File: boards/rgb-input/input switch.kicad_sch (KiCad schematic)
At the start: 5 parts, among them J1 Conn_01x02

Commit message: this board is going to be sick.
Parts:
- renumbered D29 to D9
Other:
- moved on the sheet: C3, D9, J1, R1, R2

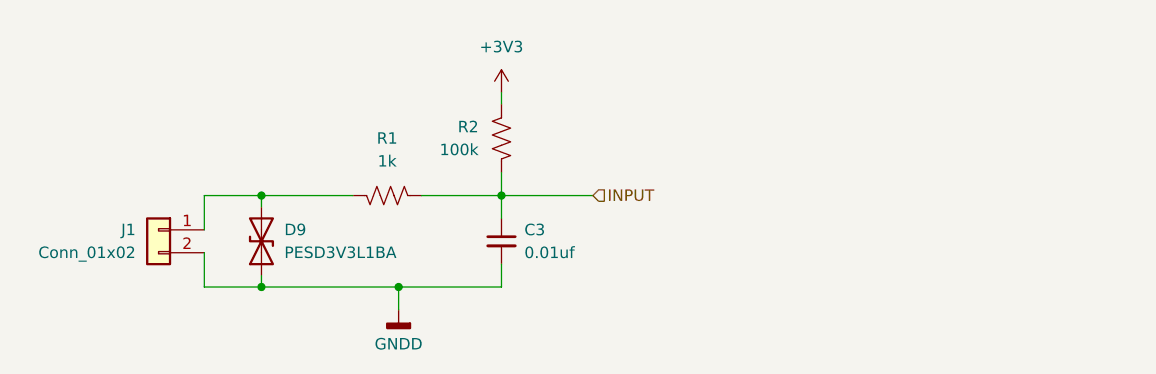
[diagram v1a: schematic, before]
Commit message: tested the bus voltage stuff a bit more
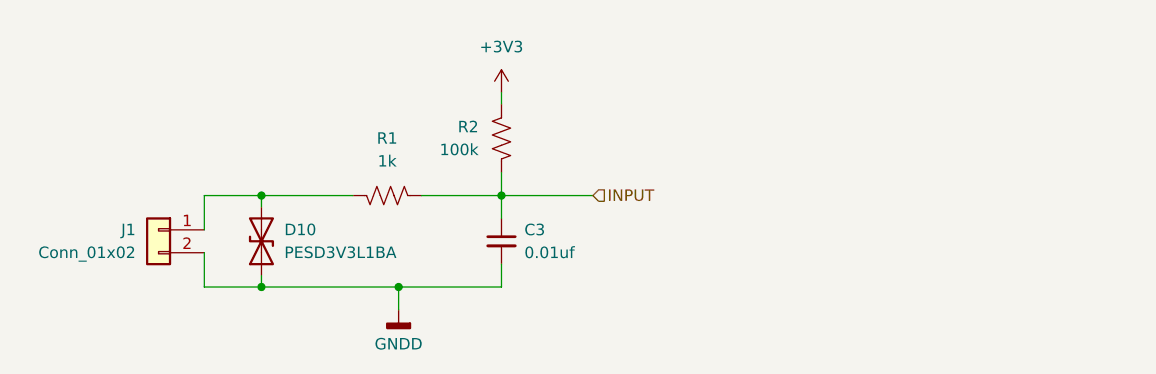
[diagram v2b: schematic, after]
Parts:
- renumbered D9 to D10
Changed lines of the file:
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@@
   (symbol (lib_id "Device:D_TVS") (at 142.24 92.075 90) (unit 1)
     (in_bom yes) (on_board yes) (dnp no)
-    (property "Reference" "D9" (at 144.78 90.805 90)
+    (property "Reference" "D10" (at 144.78 90.805 90)
       (effects (font (size 1.27 1.27)) (justify right))
     )
@@
     (instances
       (project "rgb-input"
+        (path "/c83c6236-96e9-46ad-9d7a-9e2efa4a7966/a581b924-afd8-4b56-b69e-790286072066"
+          (reference "D10") (unit 1)
+        )
+        (path "/c83c6236-96e9-46ad-9d7a-9e2efa4a7966/ef548cdc-9d5d-4f8e-8f54-0c2e96dbe3f0"
+          (reference "D2") (unit 1)
+        )
+        (path "/c83c6236-96e9-46ad-9d7a-9e2efa4a7966/4f50afed-9381-4977-8e27-209f0f88ad4e"
+          (reference "D3") (unit 1)
+        )
+        (path "/c83c6236-96e9-46ad-9d7a-9e2efa4a7966/4175a172-5c0b-4d6a-88bb-129f5f07b813"
+          (reference "D4") (unit 1)
+        )
+        (path "/c83c6236-96e9-46ad-9d7a-9e2efa4a7966/6f6f2d8d-82f6-4691-bba7-8caa1bd52e96"
+          (reference "D5") (unit 1)
+        )
+        (path "/c83c6236-96e9-46ad-9d7a-9e2efa4a7966/145fa34f-e19e-43e2-bb48-aff2e824ef0a"
+          (reference "D6") (unit 1)
+        )
+        (path "/c83c6236-96e9-46ad-9d7a-9e2efa4a7966/5fc618b8-7830-4bbf-bf46-7753631e9b1e"
+          (reference "D7") (unit 1)
+        )
+        (path "/c83c6236-96e9-46ad-9d7a-9e2efa4a7966/802175d5-fb4b-4457-a117-b0f397189ff7"
+          (reference "D8") (unit 1)
+        )
+        (path "/c83c6236-96e9-46ad-9d7a-9e2efa4a7966/0036d08f-39b5-4a29-8e4d-ea832b2cc879"
+          (reference "D29") (unit 1)
+        )
         (path "/c83c6236-96e9-46ad-9d7a-9e2efa4a7966/803edf1a-5825-4947-a8b9-85d3a29697e5"
           (reference "D9") (unit 1)
+        )
+        (path "/c83c6236-96e9-46ad-9d7a-9e2efa4a7966/9e6cdf4f-246e-427e-8315-a488968192f4"
+          (reference "D22") (unit 1)
+        )
+        (path "/c83c6236-96e9-46ad-9d7a-9e2efa4a7966/2c275ed9-e58a-403d-982f-79a49e483b85"
+          (reference "D21") (unit 1)
+        )
+        (path "/c83c6236-96e9-46ad-9d7a-9e2efa4a7966/cf1aab08-94c1-4bc0-914e-a74bb7fd137f"
+          (reference "D20") (unit 1)
+        )
+        (path "/c83c6236-96e9-46ad-9d7a-9e2efa4a7966/d9202946-506a-48d9-939c-5d39e3218bd0"
+          (reference "D19") (unit 1)
+        )
+        (path "/c83c6236-96e9-46ad-9d7a-9e2efa4a7966/9f4c4100-f7ad-41c6-bb30-0282b2fbed77"
+          (reference "D23") (unit 1)
+        )
+        (path "/c83c6236-96e9-46ad-9d7a-9e2efa4a7966/b28a4abb-d7c6-4d37-897c-3a1605d30be6"
+          (reference "D35") (unit 1)
         )
         (path "/c83c6236-96e9-46ad-9d7a-9e2efa4a7966/add74a42-7713-46b0-aac6-4fd9ca032b1b"
           (reference "D34") (unit 1)
         )
-        (path "/c83c6236-96e9-46ad-9d7a-9e2efa4a7966/b28a4abb-d7c6-4d37-897c-3a1605d30be6"
-          (reference "D35") (unit 1)
-        )
-        (path "/c83c6236-96e9-46ad-9d7a-9e2efa4a7966/9f4c4100-f7ad-41c6-bb30-0282b2fbed77"
-          (reference "D23") (unit 1)
-        )
-        (path "/c83c6236-96e9-46ad-9d7a-9e2efa4a7966/d9202946-506a-48d9-939c-5d39e3218bd0"
-          (reference "D19") (unit 1)
-        )
-        (path "/c83c6236-96e9-46ad-9d7a-9e2efa4a7966/cf1aab08-94c1-4bc0-914e-a74bb7fd137f"
-          (reference "D20") (unit 1)
-        )
-        (path "/c83c6236-96e9-46ad-9d7a-9e2efa4a7966/2c275ed9-e58a-403d-982f-79a49e483b85"
-          (reference "D21") (unit 1)
-        )
-        (path "/c83c6236-96e9-46ad-9d7a-9e2efa4a7966/9e6cdf4f-246e-427e-8315-a488968192f4"
-          (reference "D22") (unit 1)
-        )
-        (path "/c83c6236-96e9-46ad-9d7a-9e2efa4a7966/a581b924-afd8-4b56-b69e-790286072066"
-          (reference "D10") (unit 1)
-        )
-        (path "/c83c6236-96e9-46ad-9d7a-9e2efa4a7966/0036d08f-39b5-4a29-8e4d-ea832b2cc879"
-          (reference "D29") (unit 1)
-        )
-        (path "/c83c6236-96e9-46ad-9d7a-9e2efa4a7966/802175d5-fb4b-4457-a117-b0f397189ff7"
-          (reference "D8") (unit 1)
-        )
-        (path "/c83c6236-96e9-46ad-9d7a-9e2efa4a7966/5fc618b8-7830-4bbf-bf46-7753631e9b1e"
-          (reference "D7") (unit 1)
-        )
-        (path "/c83c6236-96e9-46ad-9d7a-9e2efa4a7966/145fa34f-e19e-43e2-bb48-aff2e824ef0a"
-          (reference "D6") (unit 1)
-        )
-        (path "/c83c6236-96e9-46ad-9d7a-9e2efa4a7966/6f6f2d8d-82f6-4691-bba7-8caa1bd52e96"
-          (reference "D5") (unit 1)
-        )
-        (path "/c83c6236-96e9-46ad-9d7a-9e2efa4a7966/4175a172-5c0b-4d6a-88bb-129f5f07b813"
-          (reference "D4") (unit 1)
-        )
-        (path "/c83c6236-96e9-46ad-9d7a-9e2efa4a7966/4f50afed-9381-4977-8e27-209f0f88ad4e"
-          (reference "D3") (unit 1)
-        )
-        (path "/c83c6236-96e9-46ad-9d7a-9e2efa4a7966/ef548cdc-9d5d-4f8e-8f54-0c2e96dbe3f0"
-          (reference "D2") (unit 1)
-        )
       )

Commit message: some adc changes and then rerouting
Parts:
- renumbered D10 to D9
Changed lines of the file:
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@@
   (symbol (lib_id "Device:D_TVS") (at 142.24 92.075 90) (unit 1)
     (in_bom yes) (on_board yes) (dnp no)
-    (property "Reference" "D10" (at 144.78 90.805 90)
+    (property "Reference" "D9" (at 144.78 90.805 90)
       (effects (font (size 1.27 1.27)) (justify right))
     )
@@
     (instances
       (project "rgb-input"
-        (path "/c83c6236-96e9-46ad-9d7a-9e2efa4a7966/a581b924-afd8-4b56-b69e-790286072066"
-          (reference "D10") (unit 1)
+        (path "/c83c6236-96e9-46ad-9d7a-9e2efa4a7966/803edf1a-5825-4947-a8b9-85d3a29697e5"
+          (reference "D9") (unit 1)
         )
         (path "/c83c6236-96e9-46ad-9d7a-9e2efa4a7966/ef548cdc-9d5d-4f8e-8f54-0c2e96dbe3f0"
@@
           (reference "D8") (unit 1)
         )
+        (path "/c83c6236-96e9-46ad-9d7a-9e2efa4a7966/a581b924-afd8-4b56-b69e-790286072066"
+          (reference "D10") (unit 1)
+        )
         (path "/c83c6236-96e9-46ad-9d7a-9e2efa4a7966/0036d08f-39b5-4a29-8e4d-ea832b2cc879"
           (reference "D29") (unit 1)
         )
-        (path "/c83c6236-96e9-46ad-9d7a-9e2efa4a7966/803edf1a-5825-4947-a8b9-85d3a29697e5"
-          (reference "D9") (unit 1)
-        )
         (path "/c83c6236-96e9-46ad-9d7a-9e2efa4a7966/9e6cdf4f-246e-427e-8315-a488968192f4"

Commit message: figured out most of the components, working on placement
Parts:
- INPUT0: renamed from J1; value Conn_01x02 -> ~
- renumbered D9 to D29
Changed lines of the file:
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@@
   (symbol (lib_id "Connector_Generic:Conn_01x02") (at 130.81 90.805 0) (mirror y) (unit 1)
     (in_bom yes) (on_board yes) (dnp no) (fields_autoplaced)
-    (property "Reference" "J1" (at 128.27 90.805 0)
-      (effects (font (size 1.27 1.27)) (justify left))
-    )
-    (property "Value" "Conn_01x02" (at 128.27 93.345 0)
+    (property "Reference" "INPUT0" (at 128.27 90.805 0)
+      (effects (font (size 1.27 1.27)) (justify left))
+    )
+    (property "Value" "~" (at 128.27 93.345 0)
       (effects (font (size 1.27 1.27)) (justify left))
     )
@@
       (project "rgb-input"
         (path "/c83c6236-96e9-46ad-9d7a-9e2efa4a7966/ef548cdc-9d5d-4f8e-8f54-0c2e96dbe3f0"
-          (reference "J1") (unit 1)
-        )
-        (path "/c83c6236-96e9-46ad-9d7a-9e2efa4a7966/4f50afed-9381-4977-8e27-209f0f88ad4e"
-          (reference "J2") (unit 1)
-        )
-        (path "/c83c6236-96e9-46ad-9d7a-9e2efa4a7966/4175a172-5c0b-4d6a-88bb-129f5f07b813"
-          (reference "J3") (unit 1)
-        )
-        (path "/c83c6236-96e9-46ad-9d7a-9e2efa4a7966/6f6f2d8d-82f6-4691-bba7-8caa1bd52e96"
-          (reference "J4") (unit 1)
-        )
-        (path "/c83c6236-96e9-46ad-9d7a-9e2efa4a7966/145fa34f-e19e-43e2-bb48-aff2e824ef0a"
-          (reference "J5") (unit 1)
-        )
-        (path "/c83c6236-96e9-46ad-9d7a-9e2efa4a7966/5fc618b8-7830-4bbf-bf46-7753631e9b1e"
-          (reference "J6") (unit 1)
-        )
-        (path "/c83c6236-96e9-46ad-9d7a-9e2efa4a7966/802175d5-fb4b-4457-a117-b0f397189ff7"
-          (reference "J7") (unit 1)
-        )
-        (path "/c83c6236-96e9-46ad-9d7a-9e2efa4a7966/803edf1a-5825-4947-a8b9-85d3a29697e5"
-          (reference "J8") (unit 1)
-        )
-        (path "/c83c6236-96e9-46ad-9d7a-9e2efa4a7966/a581b924-afd8-4b56-b69e-790286072066"
-          (reference "J9") (unit 1)
-        )
-        (path "/c83c6236-96e9-46ad-9d7a-9e2efa4a7966/9e6cdf4f-246e-427e-8315-a488968192f4"
-          (reference "J24") (unit 1)
-        )
-        (path "/c83c6236-96e9-46ad-9d7a-9e2efa4a7966/2c275ed9-e58a-403d-982f-79a49e483b85"
-          (reference "J23") (unit 1)
-        )
-        (path "/c83c6236-96e9-46ad-9d7a-9e2efa4a7966/cf1aab08-94c1-4bc0-914e-a74bb7fd137f"
-          (reference "J22") (unit 1)
-        )
-        (path "/c83c6236-96e9-46ad-9d7a-9e2efa4a7966/d9202946-506a-48d9-939c-5d39e3218bd0"
-          (reference "J21") (unit 1)
-        )
-        (path "/c83c6236-96e9-46ad-9d7a-9e2efa4a7966/9f4c4100-f7ad-41c6-bb30-0282b2fbed77"
-          (reference "J25") (unit 1)
-        )
-        (path "/c83c6236-96e9-46ad-9d7a-9e2efa4a7966/b28a4abb-d7c6-4d37-897c-3a1605d30be6"
-          (reference "J29") (unit 1)
-        )
-        (path "/c83c6236-96e9-46ad-9d7a-9e2efa4a7966/add74a42-7713-46b0-aac6-4fd9ca032b1b"
-          (reference "J28") (unit 1)
+          (reference "INPUT0") (unit 1)
+        )
+        (path "/c83c6236-96e9-46ad-9d7a-9e2efa4a7966/4f50afed-9381-4977-8e27-209f0f88ad4e"
+          (reference "INPUT1") (unit 1)
+        )
+        (path "/c83c6236-96e9-46ad-9d7a-9e2efa4a7966/4175a172-5c0b-4d6a-88bb-129f5f07b813"
+          (reference "INPUT2") (unit 1)
+        )
+        (path "/c83c6236-96e9-46ad-9d7a-9e2efa4a7966/6f6f2d8d-82f6-4691-bba7-8caa1bd52e96"
+          (reference "INPUT3") (unit 1)
+        )
+        (path "/c83c6236-96e9-46ad-9d7a-9e2efa4a7966/145fa34f-e19e-43e2-bb48-aff2e824ef0a"
+          (reference "INPUT4") (unit 1)
+        )
+        (path "/c83c6236-96e9-46ad-9d7a-9e2efa4a7966/5fc618b8-7830-4bbf-bf46-7753631e9b1e"
+          (reference "INPUT5") (unit 1)
+        )
+        (path "/c83c6236-96e9-46ad-9d7a-9e2efa4a7966/802175d5-fb4b-4457-a117-b0f397189ff7"
+          (reference "INPUT6") (unit 1)
+        )
+        (path "/c83c6236-96e9-46ad-9d7a-9e2efa4a7966/803edf1a-5825-4947-a8b9-85d3a29697e5"
+          (reference "INPUT7") (unit 1)
+        )
+        (path "/c83c6236-96e9-46ad-9d7a-9e2efa4a7966/a581b924-afd8-4b56-b69e-790286072066"
+          (reference "INPUT8") (unit 1)
+        )
+        (path "/c83c6236-96e9-46ad-9d7a-9e2efa4a7966/9e6cdf4f-246e-427e-8315-a488968192f4"
+          (reference "INPUT9") (unit 1)
+        )
+        (path "/c83c6236-96e9-46ad-9d7a-9e2efa4a7966/2c275ed9-e58a-403d-982f-79a49e483b85"
+          (reference "INPUT10") (unit 1)
+        )
+        (path "/c83c6236-96e9-46ad-9d7a-9e2efa4a7966/cf1aab08-94c1-4bc0-914e-a74bb7fd137f"
+          (reference "INPUT11") (unit 1)
+        )
+        (path "/c83c6236-96e9-46ad-9d7a-9e2efa4a7966/d9202946-506a-48d9-939c-5d39e3218bd0"
+          (reference "INPUT12") (unit 1)
+        )
+        (path "/c83c6236-96e9-46ad-9d7a-9e2efa4a7966/9f4c4100-f7ad-41c6-bb30-0282b2fbed77"
+          (reference "INPUT13") (unit 1)
+        )
+        (path "/c83c6236-96e9-46ad-9d7a-9e2efa4a7966/b28a4abb-d7c6-4d37-897c-3a1605d30be6"
+          (reference "INPUT14") (unit 1)
+        )
+        (path "/c83c6236-96e9-46ad-9d7a-9e2efa4a7966/add74a42-7713-46b0-aac6-4fd9ca032b1b"
+          (reference "INPUT15") (unit 1)
         )
       )
@@
   (symbol (lib_id "Device:D_TVS") (at 142.24 92.075 90) (unit 1)
     (in_bom yes) (on_board yes) (dnp no)
-    (property "Reference" "D9" (at 144.78 90.805 90)
+    (property "Reference" "D29" (at 144.78 90.805 90)
       (effects (font (size 1.27 1.27)) (justify right))
     )
@@
     (instances
       (project "rgb-input"
-        (path "/c83c6236-96e9-46ad-9d7a-9e2efa4a7966/803edf1a-5825-4947-a8b9-85d3a29697e5"
-          (reference "D9") (unit 1)
-        )
-        (path "/c83c6236-96e9-46ad-9d7a-9e2efa4a7966/ef548cdc-9d5d-4f8e-8f54-0c2e96dbe3f0"
-          (reference "D2") (unit 1)
-        )
-        (path "/c83c6236-96e9-46ad-9d7a-9e2efa4a7966/4f50afed-9381-4977-8e27-209f0f88ad4e"
-          (reference "D3") (unit 1)
-        )
-        (path "/c83c6236-96e9-46ad-9d7a-9e2efa4a7966/4175a172-5c0b-4d6a-88bb-129f5f07b813"
-          (reference "D4") (unit 1)
-        )
-        (path "/c83c6236-96e9-46ad-9d7a-9e2efa4a7966/6f6f2d8d-82f6-4691-bba7-8caa1bd52e96"
-          (reference "D5") (unit 1)
-        )
-        (path "/c83c6236-96e9-46ad-9d7a-9e2efa4a7966/145fa34f-e19e-43e2-bb48-aff2e824ef0a"
-          (reference "D6") (unit 1)
-        )
-        (path "/c83c6236-96e9-46ad-9d7a-9e2efa4a7966/5fc618b8-7830-4bbf-bf46-7753631e9b1e"
-          (reference "D7") (unit 1)
-        )
-        (path "/c83c6236-96e9-46ad-9d7a-9e2efa4a7966/802175d5-fb4b-4457-a117-b0f397189ff7"
-          (reference "D8") (unit 1)
-        )
-        (path "/c83c6236-96e9-46ad-9d7a-9e2efa4a7966/a581b924-afd8-4b56-b69e-790286072066"
-          (reference "D10") (unit 1)
-        )
         (path "/c83c6236-96e9-46ad-9d7a-9e2efa4a7966/0036d08f-39b5-4a29-8e4d-ea832b2cc879"
           (reference "D29") (unit 1)
         )
-        (path "/c83c6236-96e9-46ad-9d7a-9e2efa4a7966/9e6cdf4f-246e-427e-8315-a488968192f4"
+        (path "/c83c6236-96e9-46ad-9d7a-9e2efa4a7966/ef548cdc-9d5d-4f8e-8f54-0c2e96dbe3f0"
+          (reference "D2") (unit 1)
+        )
+        (path "/c83c6236-96e9-46ad-9d7a-9e2efa4a7966/4f50afed-9381-4977-8e27-209f0f88ad4e"
+          (reference "D3") (unit 1)
+        )
+        (path "/c83c6236-96e9-46ad-9d7a-9e2efa4a7966/4175a172-5c0b-4d6a-88bb-129f5f07b813"
+          (reference "D4") (unit 1)
+        )
+        (path "/c83c6236-96e9-46ad-9d7a-9e2efa4a7966/6f6f2d8d-82f6-4691-bba7-8caa1bd52e96"
+          (reference "D5") (unit 1)
+        )
+        (path "/c83c6236-96e9-46ad-9d7a-9e2efa4a7966/145fa34f-e19e-43e2-bb48-aff2e824ef0a"
+          (reference "D6") (unit 1)
+        )
+        (path "/c83c6236-96e9-46ad-9d7a-9e2efa4a7966/5fc618b8-7830-4bbf-bf46-7753631e9b1e"
+          (reference "D7") (unit 1)
+        )
+        (path "/c83c6236-96e9-46ad-9d7a-9e2efa4a7966/802175d5-fb4b-4457-a117-b0f397189ff7"
+          (reference "D8") (unit 1)
+        )
+        (path "/c83c6236-96e9-46ad-9d7a-9e2efa4a7966/803edf1a-5825-4947-a8b9-85d3a29697e5"
+          (reference "D9") (unit 1)
+        )
+        (path "/c83c6236-96e9-46ad-9d7a-9e2efa4a7966/a581b924-afd8-4b56-b69e-790286072066"
+          (reference "D10") (unit 1)
+        )
+        (path "/c83c6236-96e9-46ad-9d7a-9e2efa4a7966/9e6cdf4f-246e-427e-8315-a488968192f4"
